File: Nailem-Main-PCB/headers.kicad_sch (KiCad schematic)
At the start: 29 parts, among them J11 12VIN, J12 J_SR04, J13 J_DS18B20_1, J14 J_DS18B20_2, J15 J_DS18B20_3, J16 J_DS18B20_4, J17 J_STATUS, J18 J_SERVO, J19 J_TURBIDITY, J20 5VIN, J21 J_TDS, J22 J_PH, J24 J_5V_LCD, J25 J_5V_NEXTION, J26 J_3V3_LUX, J27 J_SERVO2, J28 J_ENDS, J29 5VPI

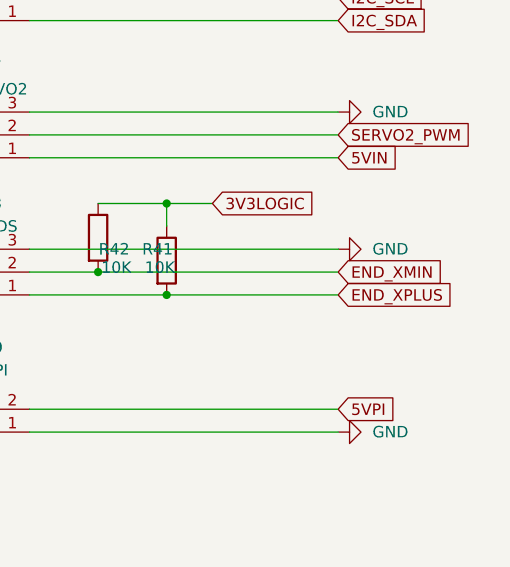
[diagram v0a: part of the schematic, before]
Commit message: Finalize PCB
PCB complete, and is currently being produced under JLCPCB with files in 'Production files for PCB'
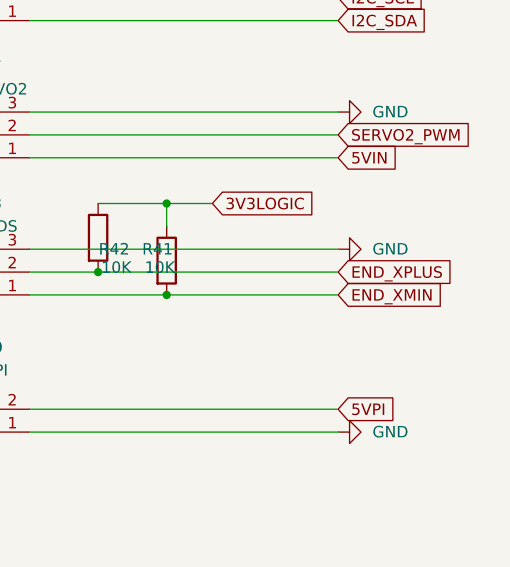
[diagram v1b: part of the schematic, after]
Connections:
- net END_XMIN: now also J28.1 (Pin_1), R42.2; no longer J28.2 (Pin_2), R41.2
- net END_XPLUS: now also J28.2 (Pin_2), R41.2; no longer J28.1 (Pin_1), R42.2
